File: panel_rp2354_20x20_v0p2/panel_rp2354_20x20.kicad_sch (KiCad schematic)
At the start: 0 parts

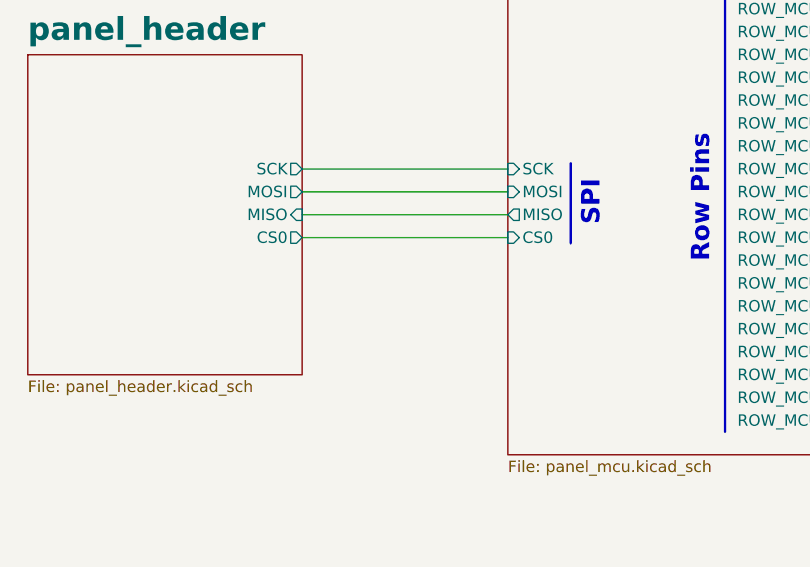
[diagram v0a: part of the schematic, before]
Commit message: Route EINT and add MISO resistor
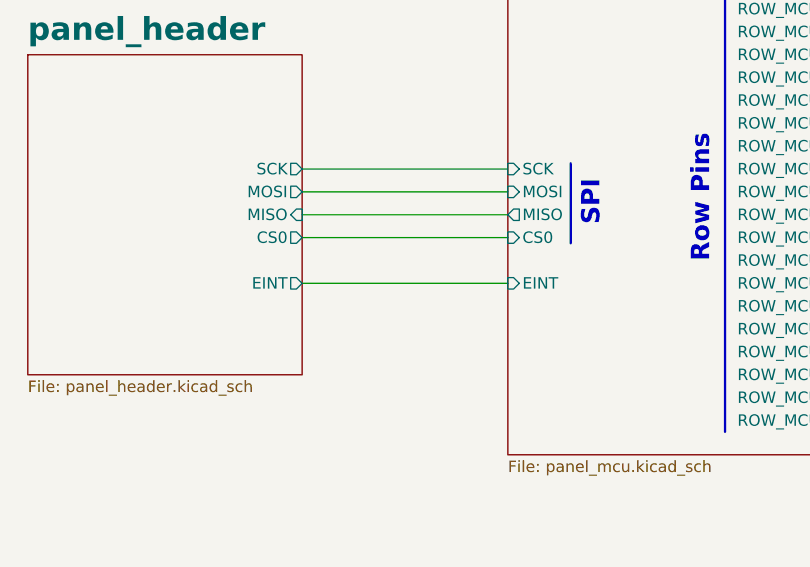
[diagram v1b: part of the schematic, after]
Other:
- sheet panel_header ports: added EINT; removed none
- sheet panel_mcu ports: added EINT; removed none
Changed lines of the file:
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@@
+	(wire
+		(pts
+			(xy 60.96 132.08) (xy 83.82 132.08)
+		)
+		(stroke
+			(width 0)
+			(type default)
+		)
+	)
 	(wire
 		(pts
@@
 			)
 		)
+		(pin "EINT" output
+			(at 60.96 132.08 0)
+			(effects
+				(font
+					(size 1.27 1.27)
+				)
+				(justify right)
+			)
+		)
 		(instances
 			(project "panel_rp2354_20x20"
@@
 			)
 		)
+		(pin "EINT" input
+			(at 83.82 132.08 180)
+			(effects
+				(font
+					(size 1.27 1.27)
+				)
+				(justify left)
+			)
+		)
